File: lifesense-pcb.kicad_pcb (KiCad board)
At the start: 2 copper layers, 4 parts, among them IC1 CC3000

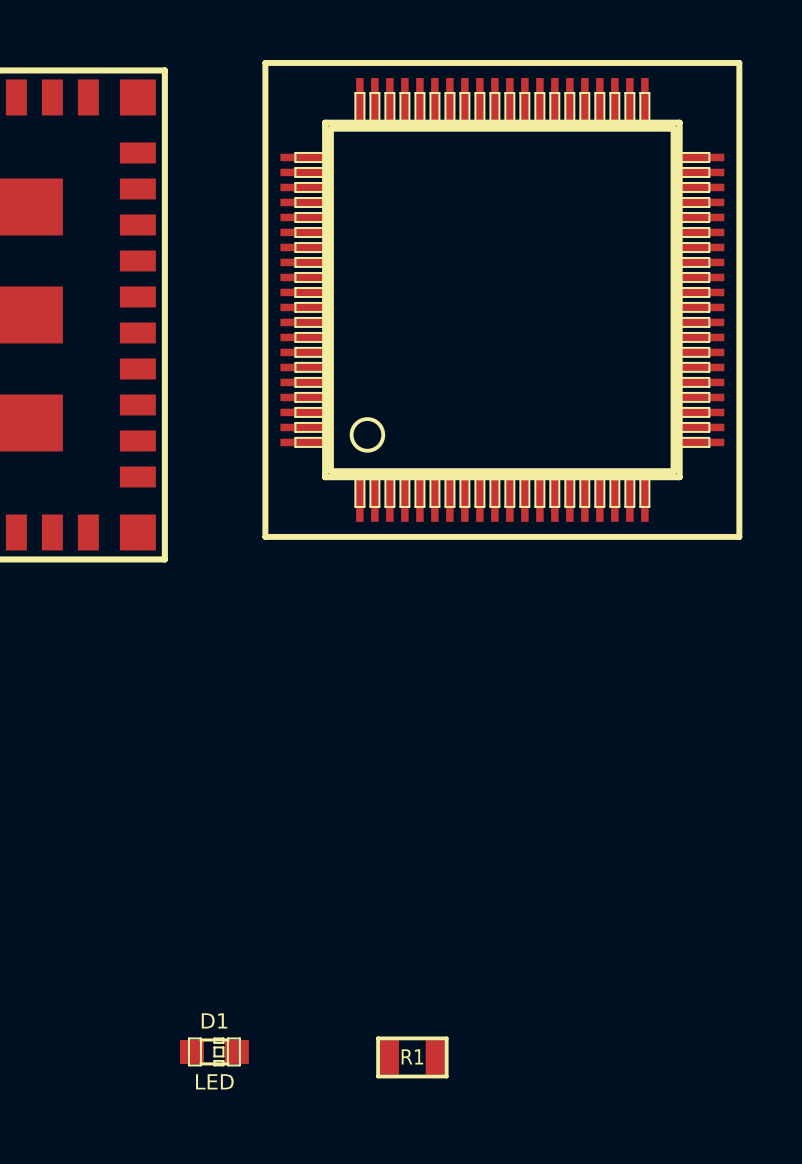
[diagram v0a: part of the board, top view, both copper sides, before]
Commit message: moving to tiva-c TM4C123GH6PM chip
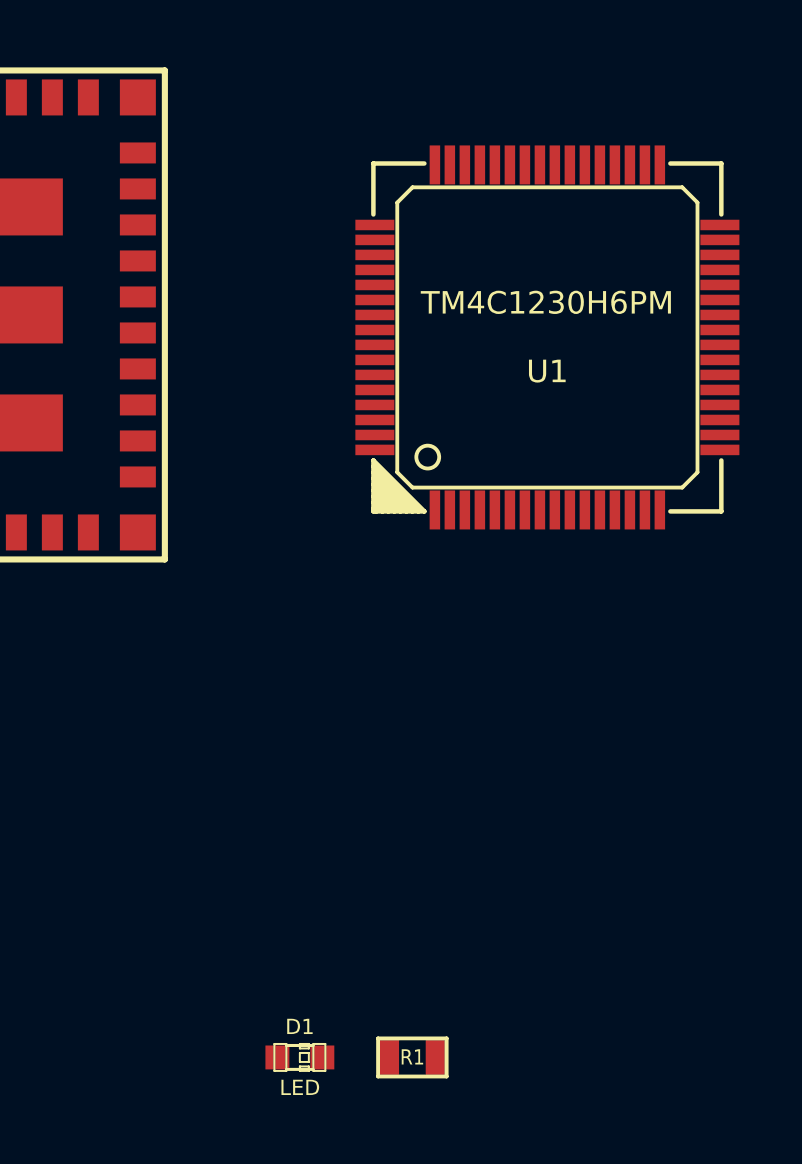
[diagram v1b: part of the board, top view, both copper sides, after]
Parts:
- removed ??1: MSP430F5529, texas-addition:texas-PN_S-PQFP-G80
- added U1: TM4C1230H6PM, QFP:lqfp64, F.Cu at (161.5, 83.0)
- moved D1 2.85 mm to (153.2, 107.0)

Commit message: only 2 things wrong, missing button
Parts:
- added A1: ANT, lifesense:ant_Wigle_A2_4G, F.Cu at (167.6, 78.8)
- added C10: 0.01uF, lifesense:SMD-0603_c, F.Cu at (144.0, 111.3)
- added C100: 4.7uF, lifesense:SMD-0603_c, F.Cu at (146.6, 87.3)
- added C101: 1pF, lifesense:SMD-0603_c, F.Cu at (165.4, 78.2)
- added C102: 100nF, lifesense:SMD-0603_c, F.Cu at (150.5, 88.5)
- added C11: 0.01uF, lifesense:SMD-0603_c, F.Cu at (161.0, 99.3)
- added C12: 1.0uF, lifesense:SMD-0603_c, F.Cu at (144.0, 112.8)
- added C14: 1.0uF, lifesense:SMD-0603_c, F.Cu at (136.7, 81.3)
- added C18: 0.01uF, lifesense:SMD-0603_c, F.Cu at (143.4, 81.0)
- added C22: 2.2uF, lifesense:SMD-0603_c, F.Cu at (161.0, 97.9)
- added C28: 24pF, lifesense:SMD-0603_c, F.Cu at (147.6, 90.8)
- added C29: 24pF, lifesense:SMD-0603_c, F.Cu at (147.6, 93.7)
- added C3: 0.01uF, lifesense:SMD-0603_c, F.Cu at (161.1, 100.8)
- added C31: 10pF, lifesense:SMD-0603_c, F.Cu at (139.0, 98.5)
- added C32: 10pF, lifesense:SMD-0603_c, F.Cu at (145.4, 98.5)
- added C4: 0.1uF, lifesense:SMD-0603_c, F.Cu at (144.0, 109.8)
- added C5: 0.01uF, lifesense:SMD-0603_c, F.Cu at (156.2, 115.4)
- added C6: 0.1uF, lifesense:SMD-0603_c, F.Cu at (161.8, 112.3)
- added C7: 1.0uF, lifesense:SMD-0603_c, F.Cu at (142.0, 100.2)
- added C8: 0.01uF, lifesense:SMD-0603_c, F.Cu at (156.2, 116.8)
- added CON1: USB-MINI-B, lifesense:ZX62-AB-5PA(11), F.Cu at (131.2, 87.2)
- added D2: LED, LEDs:LED-0805, F.Cu at (163.9, 89.5)
- added D3: LED, LEDs:LED-0805, F.Cu at (164.1, 93.6)
- added D4: Green, LEDs:LED-0805, F.Cu at (145.1, 83.8)
- added J1: CONN_10X2, Pin_Headers:Pin_Header_Straight_2x10, F.Cu at (132.1, 107.5)
- added J4: CONN_10X2, Pin_Headers:Pin_Header_Straight_2x10, F.Cu at (172.8, 108.1)
- added P1: CONN_6, Pin_Headers:Pin_Header_Straight_1x06, F.Cu at (137.7, 75.1)
- added P2: CONN_01X01, lifesense:Pin_Header_Straight_1x01, F.Cu at (158.1, 98.9)
- added P21: CONN_01X01, lifesense:Pin_Header_Straight_1x01, F.Cu at (151.9, 92.0)
- added Q1: DTC114E, lifesense:DTC114EET1G, F.Cu at (156.5, 94.0)
- added Q2: DTC114E, lifesense:DTC114EET1G, F.Cu at (156.3, 89.0)
- added Q3: DTC114E, lifesense:DTC114EET1G, F.Cu at (156.5, 91.4)
- added R10: R, lifesense:SMD-0603_r, F.Cu at (151.9, 115.9)
- added R11: R, lifesense:SMD-0603_r, F.Cu at (166.0, 96.7)
- added R12: R, lifesense:SMD-0603_r, F.Cu at (166.1, 98.5)
- added R13: 0, lifesense:SMD-0603_r, F.Cu at (152.9, 118.6)
- added R14: R, lifesense:SMD-0603_r, F.Cu at (133.9, 79.8)
- added R2: R, lifesense:SMD-0603_r, F.Cu at (152.8, 94.2)
- added R25: R, lifesense:SMD-0603_r, F.Cu at (140.3, 89.7)
- added R26: R, lifesense:SMD-0603_r, F.Cu at (142.0, 98.5)
- added R27: 330, lifesense:SMD-0603_r, F.Cu at (142.3, 84.0)
- added R28: 10K, lifesense:SMD-0603_r, F.Cu at (147.6, 97.2)
- added R29: R, lifesense:SMD-0603_r, F.Cu at (136.7, 79.7)
- added R3: 330, lifesense:SMD-0603_r, F.Cu at (160.2, 93.6)
- added R31: 1M, lifesense:SMD-0603_r, F.Cu at (153.8, 97.0)
- added R4: 330, lifesense:SMD-0603_r, F.Cu at (160.3, 89.4)
- added R5: 330, lifesense:SMD-0603_r, F.Cu at (160.3, 91.4)
- added R8: 330, lifesense:SMD-0603_r, F.Cu at (165.4, 117.0)
- added R9: R, lifesense:SMD-0603_r, F.Cu at (148.2, 115.5)
- added U2: TPS73633DRB, lifesense:TPS73633DBV, F.Cu at (137.2, 84.1)
- added Y1: CRYSTAL, lifesense:AB26TRB, F.Cu at (141.8, 91.8)
- added Y2: CRYSTAL, lifesense:ABM3, F.Cu at (143.0, 96.0)
- D1: footprint LEDs:LED-0603 -> LEDs:LED-0805
- R1: value R -> 0; footprint SMD_Packages:SM0603 -> lifesense:SMD-0603_r
- U1: value TM4C1230H6PM -> TM4C123GH6PM; footprint QFP:lqfp64 -> lifesense:lqfp64
- moved U1 25.6 mm to (152.3, 106.8), turned to 45 degrees
- moved D1 18.8 mm to (164.0, 91.5)
- moved IC1 13.9 mm to (155.8, 80.8), turned to 270 degrees
- moved R1 10.4 mm to (165.9, 101.7)
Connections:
- D1 pad 1: VCC -> Net-(D1-Pad1)
- D1 pad 2: Net-(D1-Pad2) -> GND
- IC1 pad 1: Net-(IC1-Pad1) -> GND
- IC1 pad 10: Net-(IC1-Pad10) -> GND
- IC1 pad 11: Net-(IC1-Pad11) -> GND
- IC1 pad 12: Net-(IC1-Pad12) -> /PE0
- IC1 pad 13: Net-(IC1-Pad13) -> /MISO
- IC1 pad 14: Net-(IC1-Pad14) -> /PB2
- IC1 pad 15: Net-(IC1-Pad15) -> /MOSI
- IC1 pad 16: Net-(IC1-Pad16) -> GND
- IC1 pad 17: Net-(IC1-Pad17) -> /PB4
- IC1 pad 18: Net-(IC1-Pad18) -> GND
- IC1 pad 19: Net-(IC1-Pad19) -> +3.3V
- IC1 pad 20: Net-(IC1-Pad20) -> GND
- IC1 pad 21: Net-(IC1-Pad21) -> GND
- IC1 pad 22: Net-(IC1-Pad22) -> GND
- IC1 pad 23: Net-(IC1-Pad23) -> +3.3V
- IC1 pad 25: Net-(IC1-Pad25) -> GND
- IC1 pad 26: Net-(IC1-Pad26) -> /PB5
- IC1 pad 31: Net-(IC1-Pad31) -> GND
- IC1 pad 32: Net-(IC1-Pad32) -> GND
- IC1 pad 33: Net-(IC1-Pad33) -> GND
- IC1 pad 34: Net-(IC1-Pad34) -> GND
- IC1 pad 36: Net-(IC1-Pad36) -> GND
- IC1 pad 37: Net-(IC1-Pad37) -> GND
- IC1 pad 38: Net-(IC1-Pad38) -> GND
- IC1 pad 39: Net-(IC1-Pad39) -> GND
- IC1 pad 40: Net-(IC1-Pad40) -> GND
- IC1 pad 41: Net-(IC1-Pad41) -> GND
- IC1 pad 42: Net-(IC1-Pad42) -> GND
- IC1 pad 43: Net-(IC1-Pad43) -> GND
- IC1 pad 44: Net-(IC1-Pad44) -> GND
- IC1 pad 45: Net-(IC1-Pad45) -> GND
- IC1 pad 46: Net-(IC1-Pad46) -> GND
- IC1 pad 7: Net-(IC1-Pad7) -> Net-(IC1-Pad5)
- IC1 pad 9: Net-(IC1-Pad9) -> GND
- R1 pad 1: Net-(D1-Pad2) -> Net-(R1-Pad1)
- R1 pad 2: GND -> /USR_SW2
- U1 pad 1: Net-(U1-Pad1) -> /MISO
- U1 pad 10: Net-(U1-Pad10) -> /PD7
- U1 pad 11: Net-(U1-Pad11) -> +3.3V
- U1 pad 12: Net-(U1-Pad12) -> GND
- U1 pad 13: Net-(U1-Pad13) -> /PC7
- U1 pad 14: Net-(U1-Pad14) -> /PC6
- U1 pad 15: Net-(U1-Pad15) -> /PC5
- U1 pad 16: Net-(U1-Pad16) -> /PC4
- U1 pad 17: Net-(U1-Pad17) -> /PA0
- U1 pad 18: Net-(U1-Pad18) -> /PA1
- U1 pad 19: Net-(U1-Pad19) -> /PA2
- U1 pad 2: Net-(U1-Pad2) -> +3.3V
- U1 pad 20: Net-(U1-Pad20) -> /PA3
- U1 pad 21: Net-(U1-Pad21) -> /PA4
- U1 pad 22: Net-(U1-Pad22) -> /PA5
- U1 pad 23: Net-(U1-Pad23) -> /PA6
- U1 pad 24: Net-(U1-Pad24) -> /PA7
- U1 pad 25: Net-(U1-Pad25) -> MCU_VDDC
- U1 pad 26: Net-(U1-Pad26) -> +3.3V
- U1 pad 27: Net-(U1-Pad27) -> GND
- U1 pad 28: Net-(U1-Pad28) -> /PF0
- U1 pad 29: Net-(U1-Pad29) -> /LED_R
- U1 pad 3: Net-(U1-Pad3) -> GND
- U1 pad 30: Net-(U1-Pad30) -> /LED_B
- U1 pad 31: Net-(U1-Pad31) -> /LED_G
- U1 pad 32: Net-(U1-Pad32) -> /~WAKE~
- U1 pad 33: Net-(U1-Pad33) -> /~HIB~
- U1 pad 37: Net-(U1-Pad37) -> +3.3V
- U1 pad 38: Net-(U1-Pad38) -> /~RST~
- U1 pad 39: Net-(U1-Pad39) -> GND
- U1 pad 4: Net-(U1-Pad4) -> /MOSI
- U1 pad 42: Net-(U1-Pad42) -> +3.3V
- U1 pad 43: Net-(U1-Pad43) -> /USB_DM
- U1 pad 44: Net-(U1-Pad44) -> /USB_DP
- U1 pad 45: Net-(U1-Pad45) -> /PB0
- U1 pad 46: Net-(U1-Pad46) -> /PB1
- U1 pad 47: Net-(U1-Pad47) -> /PB2
- U1 pad 48: Net-(U1-Pad48) -> /PB3
- U1 pad 49: Net-(U1-Pad49) -> /PC3
- U1 pad 5: Net-(U1-Pad5) -> /PF4
- U1 pad 50: Net-(U1-Pad50) -> /PC2
- U1 pad 51: Net-(U1-Pad51) -> /PC1
- U1 pad 52: Net-(U1-Pad52) -> /PC0
- U1 pad 53: Net-(U1-Pad53) -> /PD6
- U1 pad 54: Net-(U1-Pad54) -> +3.3V
- U1 pad 55: Net-(U1-Pad55) -> GND
- U1 pad 56: Net-(U1-Pad56) -> MCU_VDDC
- U1 pad 57: Net-(U1-Pad57) -> /PB5
- U1 pad 58: Net-(U1-Pad58) -> /PB4
- U1 pad 59: Net-(U1-Pad59) -> /PE4
- U1 pad 6: Net-(U1-Pad6) -> /PE3
- U1 pad 60: Net-(U1-Pad60) -> /PE5
- U1 pad 61: Net-(U1-Pad61) -> /MISO
- U1 pad 62: Net-(U1-Pad62) -> /MOSI
- U1 pad 63: Net-(U1-Pad63) -> /PD2
- U1 pad 64: Net-(U1-Pad64) -> /PD3
- U1 pad 7: Net-(U1-Pad7) -> /PE2
- U1 pad 8: Net-(U1-Pad8) -> /PE1
- U1 pad 9: Net-(U1-Pad9) -> /PE0
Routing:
- net +3.3V: track 0.00 -> 121.0 mm, vias 0 -> 6
- net /MOSI: track 0.00 -> 112.5 mm, vias 0 -> 8
- net GND: track 0.00 -> 112.1 mm, vias 0 -> 22
- net /MISO: track 0.00 -> 104.3 mm, vias 0 -> 4
- net /PB2: track 0.00 -> 87.6 mm, vias 0 -> 4
- net /PE0: track 0.00 -> 81.5 mm, vias 0 -> 2
- net /PB5: track 0.00 -> 67.8 mm, vias 0 -> 4
- net /PB4: track 0.00 -> 55.7 mm, vias 0 -> 2
- net /PB1: track 0.00 -> 48.5 mm, vias 0 -> 2
- net /PA0: track 0.00 -> 46.1 mm, vias 0 -> 1
- net /PC3: track 0.00 -> 45.8 mm, vias 0 -> 1
- net /PA1: track 0.00 -> 44.0 mm, vias 0 -> 1
- net /PE1: track 0.00 -> 43.8 mm, vias 0 -> 2
- net /PC2: track 0.00 -> 43.8 mm, vias 0 -> 1
- net /LED_R: track 0.00 -> 43.7 mm, vias 0 -> 3
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- added copper zone on B.Cu, net GND
- added copper zone on F.Cu, net GND
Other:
- net class Default: clearance 0.254 -> 0.2032; trace_width 0.254 -> 0.2032; via_drill 0.635 -> 0.508
- rule trace_clearance: 0.254 -> 0.2032
- rule trace_min: 0.254 -> 0.2032

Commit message: finished board 1.0
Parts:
- removed R1, R13: 0, lifesense:SMD-0603_r
- removed R8: 330, lifesense:SMD-0603_r
- added SW3: SW_PUSH, lifesense:B3S-1000, F.Cu at (133.9, 78.9)
- moved R2 11.5 mm to (162.9, 99.7), turned to 270 degrees
- moved U2 6.76 mm to (143.9, 83.2)
- moved C3 4.71 mm to (156.9, 98.5), turned to 270 degrees
- moved D4 4.68 mm to (144.0, 88.3), turned to 0 degrees
- moved R29 4.06 mm to (138.1, 83.5), turned to 180 degrees
- moved C14 4.01 mm to (138.1, 85.0), turned to 180 degrees
- moved R14 3.94 mm to (135.8, 83.3)
- moved R27 2.91 mm to (143.6, 86.6), turned to 180 degrees
- moved R25 2.80 mm to (137.6, 89.6)
- moved Y2 2.58 mm to (140.4, 95.8)
- moved C22 2.37 mm to (159.7, 99.8)
- moved C11 2.36 mm to (159.7, 101.3)
- moved C4 2.00 mm to (142.1, 109.2)
- moved P2 1.70 mm to (159.1, 97.6)
- moved CON1 1.47 mm to (131.2, 88.7)
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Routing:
- net GND: track 112.1 -> 217.2 mm, vias 22 -> 30
- net /LED_R: track 43.7 -> 74.1 mm, vias 3 -> 2
- net /~RST~: track 35.5 -> 65.1 mm, vias 3 -> 5
- net +3.3V: track 121.0 -> 144.9 mm, vias 6 -> 7
- net Net-(Q1-Pad1): track 3.13 -> 14.3 mm, vias 0 -> 2
- net /MOSI: track 112.5 -> 121.8 mm, vias 8 -> 7
- net /PA5: track 35.6 -> 43.7 mm, vias 1 -> 3
- net /PA6: track 34.5 -> 42.4 mm
- net /PE3: track 38.9 -> 46.7 mm
- net MCU_VDDC: track 19.7 -> 27.4 mm, vias 1 -> 2
- net USB_VBUS: track 22.8 -> 29.7 mm
- net Net-(CON1-Pad6): track 39.8 -> 33.1 mm
- net Net-(C18-Pad1): track 8.32 -> 2.75 mm
- net /PD6: track 32.1 -> 37.5 mm, vias 2 -> 4
- net /PA7: track 38.3 -> 43.4 mm, vias 1 -> 3
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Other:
- board outline added: 47 x 48.8 mm
- board text added: "Dan Willoughby"

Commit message: fabricated 1.1 version
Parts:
- U2: value TPS73633DRB -> TPS73633DBV
- moved D4 6.72 mm to (142.1, 81.8), turned to 180 degrees
- moved C18 6.24 mm to (145.6, 87.1), turned to 0 degrees
- moved C100 5.88 mm to (151.6, 90.4), turned to 0 degrees
- moved R27 4.97 mm to (145.2, 82.0), turned to 90 degrees
- moved R14 4.85 mm to (130.9, 83.9), turned to 0 degrees
- moved R29 3.85 mm to (134.3, 83.8), turned to 0 degrees
- moved P21 2.31 mm to (152.9, 94.3)
- moved U2 1.67 mm to (143.4, 84.8), turned to 270 degrees
- moved CON1 1.51 mm to (130.8, 90.2)
- moved C102 1.16 mm to (151.6, 88.8)
- moved SW3 0.89 mm to (133.8, 79.8)
- moved D2 0.46 mm to (164.4, 90.2), turned to 180 degrees
- moved D3 0.44 mm to (164.4, 93.8), turned to 180 degrees
- moved D1 0.44 mm to (164.4, 92.0), turned to 180 degrees
- moved C14 0.37 mm to (138.4, 84.9), turned to 0 degrees
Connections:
- C100 pad 1: +3.3V -> MCU_PWR
- C102 pad 1: +3.3V -> MCU_PWR
- C3 pad 1: +3.3V -> MCU_PWR
- C4 pad 1: +3.3V -> MCU_PWR
- C5 pad 1: +3.3V -> MCU_PWR
- C6 pad 1: +3.3V -> MCU_PWR
- C7 pad 1: +3.3V -> MCU_PWR
- C8 pad 1: +3.3V -> MCU_PWR
- D1 pad 1: Net-(D1-Pad1) -> USB_VBUS
- D1 pad 2: GND -> Net-(D1-Pad2)
- D2 pad 1: Net-(D2-Pad1) -> USB_VBUS
- D2 pad 2: GND -> Net-(D2-Pad2)
- D3 pad 1: Net-(D3-Pad1) -> USB_VBUS
- D3 pad 2: GND -> Net-(D3-Pad2)
- IC1 pad 19: +3.3V -> MCU_PWR
- IC1 pad 23: +3.3V -> MCU_PWR
- IC1 pad 28: Net-(IC1-Pad28) -> Net-(IC1-Pad27)
- IC1 pad 30: Net-(IC1-Pad30) -> Net-(IC1-Pad29)
- J1 pad 1: +3.3V -> MCU_PWR
- R27 pad 1: +3.3V -> MCU_PWR
- R28 pad 1: +3.3V -> MCU_PWR
- R3 pad 1: Net-(D3-Pad1) -> Net-(D3-Pad2)
- R31 pad 1: +3.3V -> MCU_PWR
- R4 pad 1: Net-(D2-Pad1) -> Net-(D2-Pad2)
- R5 pad 1: Net-(D1-Pad1) -> Net-(D1-Pad2)
- U1 pad 11: +3.3V -> MCU_PWR
- U1 pad 2: +3.3V -> MCU_PWR
- U1 pad 26: +3.3V -> MCU_PWR
- U1 pad 37: +3.3V -> MCU_PWR
- U1 pad 42: +3.3V -> MCU_PWR
- U1 pad 54: +3.3V -> MCU_PWR
- U2 pad 1: +3.3V -> USB_VBUS
- U2 pad 2: (no net) -> GND
- U2 pad 3: Net-(C18-Pad1) -> USB_VBUS
- U2 pad 4: GND -> Net-(C18-Pad1)
- U2 pad 5: USB_VBUS -> MCU_PWR
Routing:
- net MCU_PWR: track 0.00 -> 146.8 mm, vias 0 -> 7
- net +3.3V: track 144.9 -> 0.00 mm, vias 7 -> 0
- net USB_VBUS: track 29.7 -> 65.9 mm, vias 1 -> 3
- net Net-(CON1-Pad6): track 33.1 -> 16.4 mm, vias 2 -> 0
- net GND: track 217.2 -> 224.6 mm, vias 30 -> 29
- net Net-(IC1-Pad29): track 0.00 -> 3.53 mm
- net Net-(IC1-Pad27): track 0.00 -> 3.17 mm
- net /PB4: track 59.1 -> 62.2 mm
- net Net-(D2-Pad2): track 0.00 -> 2.48 mm
- net Net-(D3-Pad2): track 0.00 -> 2.44 mm
- net Net-(D1-Pad2): track 0.00 -> 2.38 mm
- net Net-(D3-Pad1): track 2.08 -> 0.00 mm
- net Net-(D2-Pad1): track 1.98 -> 0.00 mm
- net Net-(D1-Pad1): track 1.93 -> 0.00 mm
- net /~HIB~: track 8.57 -> 7.00 mm
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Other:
- board text added: "RXD"
- board text added: "Rev 1.1"
- board text added: "TCK"
- board text added: "TDI"
- board text added: "TDO"
- board text added: "TMS"
- board text added: "TXD"
